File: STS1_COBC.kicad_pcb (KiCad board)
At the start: 4 copper layers, 81 x 85 mm, 207 parts, among them J1 UHF, J16 SWD, Q1 SQ2318, Q2 BSS123, Q3 SQ2318, Q4 SQ2318, U1 W25Q01JVZEIQ, U10 TQP3M9036, U11 NL17SV04XV5T2G, U12 FPF2701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

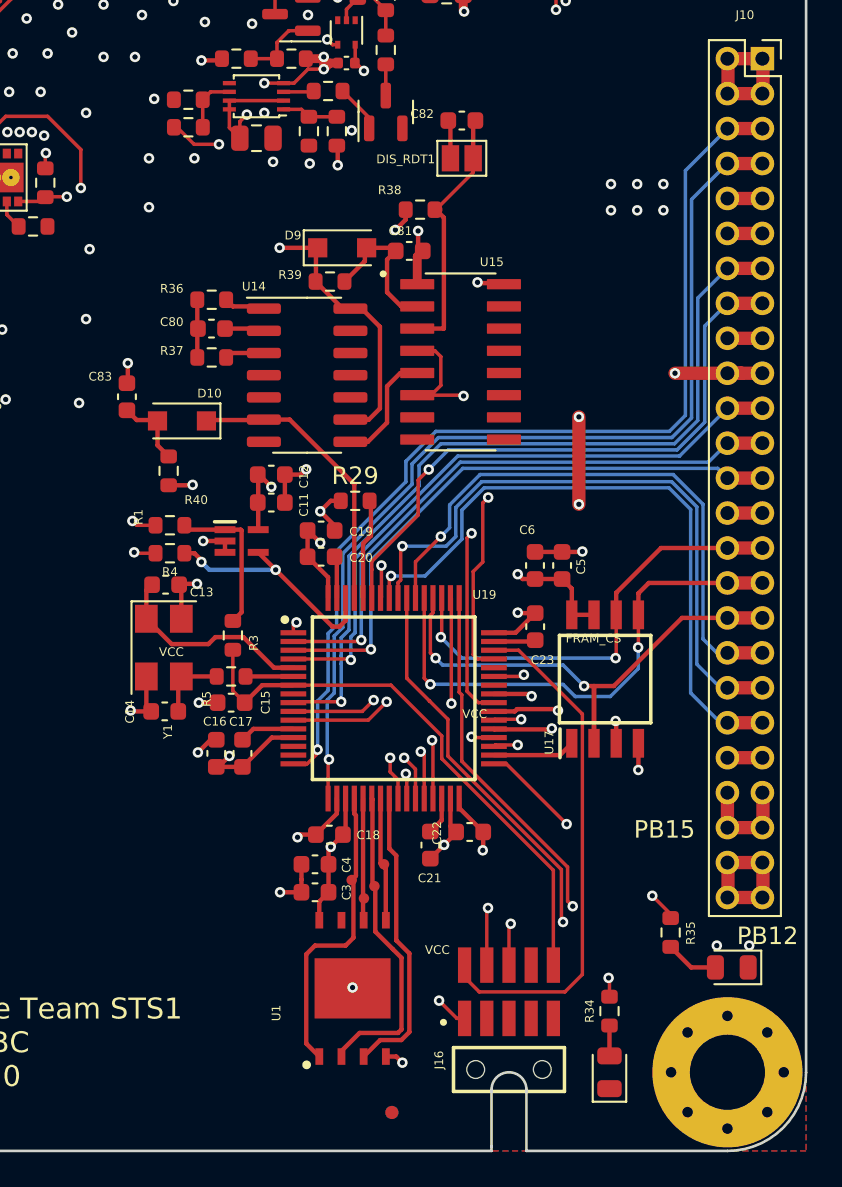
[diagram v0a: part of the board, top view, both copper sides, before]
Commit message: Reorganize silkscreen labels
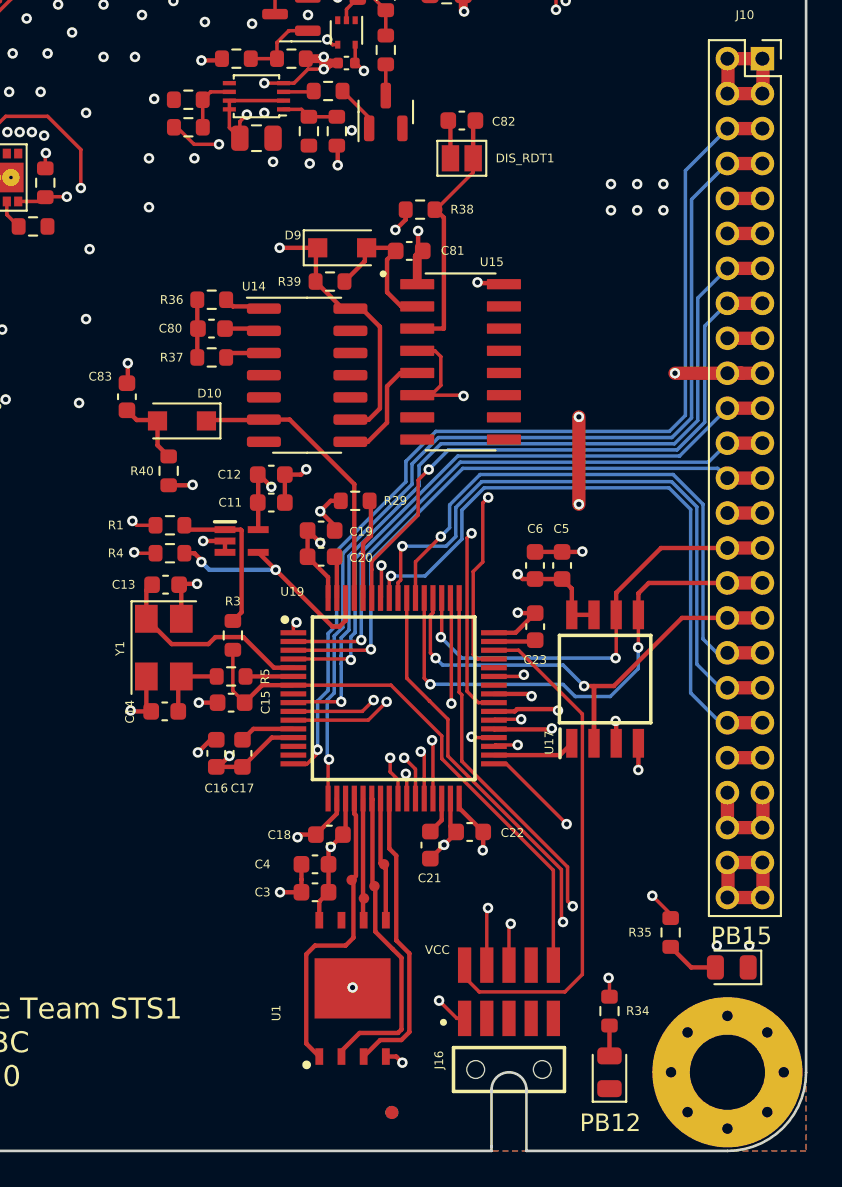
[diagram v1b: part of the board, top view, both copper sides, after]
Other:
- board text removed: "FRAM_CS"
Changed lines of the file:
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@@
     (property "Sheetname" "COBC STM")
     (attr smd)
-    (fp_text reference "Y1" (at 4.81094 -0.2344 90) (layer "F.SilkS")
+    (fp_text reference "Y1" (at 0.05 2.5 90) (layer "F.SilkS")
       (effects (font (size 0.5 0.5) (thickness 0.1)))
     )
@@
     (property "Sheetname" "COBC STM")
     (attr smd)
-    (fp_text reference "R1" (at 1.7985 0.47046 90) (layer "F.SilkS")
+    (fp_text reference "R1" (at 3.1 0 180) (layer "F.SilkS")
       (effects (font (size 0.5 0.5) (thickness 0.1)))
     )
@@
     (property "Sheetname" "COBC STM")
     (attr smd)
-    (fp_text reference "R3" (at 0.43246 -1.1965 90) (layer "F.SilkS")
+    (fp_text reference "R3" (at -1.95 0 180) (layer "F.SilkS")
       (effects (font (size 0.5 0.5) (thickness 0.1)))
     )
@@
     (property "Sheetname" "COBC STM")
     (attr smd)
-    (fp_text reference "C22" (at 1.8655 -0.05746 90) (layer "F.SilkS")
+    (fp_text reference "C22" (at -2.45 -0.05 180) (layer "F.SilkS")
       (effects (font (size 0.5 0.5) (thickness 0.1)))
     )
@@
     (property "Sheetname" "Resetdog")
     (attr smd)
-    (fp_text reference "R37" (at 2.286 0.381) (layer "F.SilkS")
+    (fp_text reference "R37" (at 2.29 -0.0035) (layer "F.SilkS")
       (effects (font (size 0.5 0.5) (thickness 0.1)))
     )
@@
     (property "Sheetname" "Resetdog")
     (attr smd)
-    (fp_text reference "C81" (at -0.508 -1.143) (layer "F.SilkS")
+    (fp_text reference "C81" (at 2.487 -0.0105) (layer "F.SilkS")
       (effects (font (size 0.5 0.5) (thickness 0.1)))
     )
@@
     (property "Sheetname" "COBC STM")
     (attr smd)
-    (fp_text reference "C15" (at 1.9735 -0.01346 90) (layer "F.SilkS")
+    (fp_text reference "C15" (at 1.9735 -0.01346 270) (layer "F.SilkS")
       (effects (font (size 0.5 0.5) (thickness 0.1)))
     )
@@
     (property "Sheetname" "Resetdog")
     (attr smd)
-    (fp_text reference "C82" (at 2.273 0.381) (layer "F.SilkS")
+    (fp_text reference "C82" (at -2.398 -0.059) (layer "F.SilkS")
       (effects (font (size 0.5 0.5) (thickness 0.1)))
     )
@@
     (property "Sheetname" "Resetdog")
     (attr smd)
-    (fp_text reference "C80" (at -2.273 -0.381) (layer "F.SilkS")
+    (fp_text reference "C80" (at -2.347 -0.0055) (layer "F.SilkS")
       (effects (font (size 0.5 0.5) (thickness 0.1)))
     )
@@
     (property "Sheetname" "COBC STM")
     (attr smd)
-    (fp_text reference "C12" (at 1.8635 0.11446 90) (layer "F.SilkS")
+    (fp_text reference "C12" (at -2.4 0 180) (layer "F.SilkS")
       (effects (font (size 0.5 0.5) (thickness 0.1)))
     )
@@
     (property "Sheetname" "COBC Memories")
     (attr smd)
-    (fp_text reference "C5" (at 0.061 -1.0805 90) (layer "F.SilkS")
+    (fp_text reference "C5" (at -2.1 0.04 180) (layer "F.SilkS")
       (effects (font (size 0.5 0.5) (thickness 0.1)))
     )
@@
     (property "Sheetname" "COBC STM")
     (attr smd)
-    (fp_text reference "R34" (at 0 1.1355 90) (layer "F.SilkS")
+    (fp_text reference "R34" (at -0.01 -1.62 180) (layer "F.SilkS")
       (effects (font (size 0.5 0.5) (thickness 0.1)))
     )
@@
     (property "Sheetname" "Resetdog")
     (attr smd)
-    (fp_text reference "R38" (at -1.7394 -1.1176) (layer "F.SilkS")
+    (fp_text reference "R38" (at 2.4052 -0.0083) (layer "F.SilkS")
       (effects (font (size 0.5 0.5) (thickness 0.1)))
     )
@@
     (property "Sheetname" "COBC STM")
     (attr smd)
-    (fp_text reference "C11" (at 1.8635 0.13246 90) (layer "F.SilkS")
+    (fp_text reference "C11" (at -2.35 0 180) (layer "F.SilkS")
       (effects (font (size 0.5 0.5) (thickness 0.1)))
     )
@@
     (property "Sheetname" "Resetdog")
     (attr smd)
-    (fp_text reference "R40" (at 1.6642 -1.5748 180) (layer "F.SilkS")
+    (fp_text reference "R40" (at 0.0143 1.5262 180) (layer "F.SilkS")
       (effects (font (size 0.5 0.5) (thickness 0.1)))
     )
@@
     (property "Sheetname" "COBC Memories")
     (attr smd)
-    (fp_text reference "C3" (at 1.8065 -0.00054 90) (layer "F.SilkS")
+    (fp_text reference "C3" (at -3 0 180) (layer "F.SilkS")
       (effects (font (size 0.5 0.5) (thickness 0.1)))
     )
@@
     (property "exclude_from_bom" "")
     (attr exclude_from_pos_files exclude_from_bom)
-    (fp_text reference "DIS_RDT1" (at -3.2108 0.0529) (layer "F.SilkS")
+    (fp_text reference "DIS_RDT1" (at 3.62 0) (layer "F.SilkS")
       (effects (font (size 0.5 0.5) (thickness 0.1)))
     )
@@
     (property "Sheetname" "COBC STM")
     (attr smd)
-    (fp_text reference "R29" (at 0 -1.43) (layer "F.SilkS")
-      (effects (font (size 1 1) (thickness 0.15)))
+    (fp_text reference "R29" (at 2.3 0) (layer "F.SilkS")
+      (effects (font (size 0.5 0.5) (thickness 0.1)))
     )
     (fp_text value "10K" (at 0 1.43) (layer "F.Fab")
@@
     (property "Sheetname" "COBC STM")
     (attr smd)
-    (fp_text reference "U19" (at 5.19246 -5.925) (layer "F.SilkS")
+    (fp_text reference "U19" (at -5.8 -6.1) (layer "F.SilkS")
       (effects (font (size 0.5 0.5) (thickness 0.1)))
     )
@@
     (property "Sheetname" "COBC STM")
     (attr smd)
-    (fp_text reference "R5" (at 1.3965 -1.28754 90) (layer "F.SilkS")
+    (fp_text reference "R5" (at -1.95 0 270) (layer "F.SilkS")
       (effects (font (size 0.5 0.5) (thickness 0.1)))
     )
@@
     (property "Sheetname" "COBC STM")
     (attr smd)
-    (fp_text reference "C18" (at 2.22446 0.0295) (layer "F.SilkS")
+    (fp_text reference "C18" (at -2.865 0.02) (layer "F.SilkS")
       (effects (font (size 0.5 0.5) (thickness 0.1)))
     )
@@
     (property "Sheetname" "COBC STM")
     (attr smd)
-    (fp_text reference "R4" (at 0 -1.0685) (layer "F.SilkS")
+    (fp_text reference "R4" (at 3.1 0) (layer "F.SilkS")
       (effects (font (size 0.5 0.5) (thickness 0.1)))
     )
@@
     (property "Sheetname" "COBC STM")
     (attr smd)
-    (fp_text reference "C23" (at 1.9099 -0.41846) (layer "F.SilkS")
+    (fp_text reference "C23" (at 1.9 0) (layer "F.SilkS")
       (effects (font (size 0.5 0.5) (thickness 0.1)))
     )
@@
     (property "Sheetname" "COBC Memories")
     (attr smd)
-    (fp_text reference "C4" (at 1.8065 0.03046 90) (layer "F.SilkS")
+    (fp_text reference "C4" (at -3 0 180) (layer "F.SilkS")
       (effects (font (size 0.5 0.5) (thickness 0.1)))
     )
@@
     (property "Sheetname" "Resetdog")
     (attr smd)
-    (fp_text reference "R36" (at 2.286 0.635) (layer "F.SilkS")
+    (fp_text reference "R36" (at 2.29 -0.0055) (layer "F.SilkS")
       (effects (font (size 0.5 0.5) (thickness 0.1)))
     )
@@
     (property "Sheetname" "COBC STM")
     (attr smd)
-    (fp_text reference "C13" (at -2.06446 -0.4295 180) (layer "F.SilkS")
+    (fp_text reference "C13" (at 2.4 0 180) (layer "F.SilkS")
       (effects (font (size 0.5 0.5) (thickness 0.1)))
     )
@@
     (property "Sheetname" "Resetdog")
     (attr smd)
-    (fp_text reference "R39" (at -2.286 -0.381) (layer "F.SilkS")
+    (fp_text reference "R39" (at -2.3196 0.0069) (layer "F.SilkS")
       (effects (font (size 0.5 0.5) (thickness 0.1)))
     )
@@
     (property "Sheetname" "COBC STM")
     (attr smd)
-    (fp_text reference "R35" (at 0.035 -1.1505 90) (layer "F.SilkS")
+    (fp_text reference "R35" (at 0 1.75 180) (layer "F.SilkS")
       (effects (font (size 0.5 0.5) (thickness 0.1)))
     )
@@
     (property "Sheetname" "COBC STM")
     (attr smd)
-    (fp_text reference "C16" (at 1.8205 -0.07954 180) (layer "F.SilkS")
+    (fp_text reference "C16" (at -2 0 180) (layer "F.SilkS")
       (effects (font (size 0.5 0.5) (thickness 0.1)))
     )
@@
     (property "Sheetname" "COBC Memories")
     (attr smd)
-    (fp_text reference "C6" (at -2.032 0.4455) (layer "F.SilkS")
+    (fp_text reference "C6" (at -2.1 -0.01) (layer "F.SilkS")
       (effects (font (size 0.5 0.5) (thickness 0.1)))
     )
@@
     (property "Sheetname" "COBC STM")
     (attr smd)
-    (fp_text reference "C17" (at -1.8105 0.08754) (layer "F.SilkS")
+    (fp_text reference "C17" (at 2 0) (layer "F.SilkS")
       (effects (font (size 0.5 0.5) (thickness 0.1)))
     )
@@
     (effects (font (size 1.2 1.2) (thickness 0.2)))
   )
-  (gr_text "PB15" (at 187.898 108.6104) (layer "F.SilkS")
+  (gr_text "PB15" (at 192.3 114.7) (layer "F.SilkS")
     (effects (font (size 1 1) (thickness 0.15)))
   )
-  (gr_text "VCC" (at 177.03254 102) (layer "F.SilkS")
-    (effects (font (size 0.5 0.5) (thickness 0.1)))
-  )
-  (gr_text "FRAM_CS" (at 183.837 97.6755) (layer "F.SilkS")
-    (effects (font (size 0.5 0.5) (thickness 0.1)))
-  )
   (gr_text "3V3" (at 138.368 91.276) (layer "F.SilkS")
     (effects (font (size 1 1) (thickness 0.15)))
   )
-  (gr_text "PB12" (at 193.8 114.7) (layer "F.SilkS")
+  (gr_text "PB12" (at 184.8 125.4) (layer "F.SilkS")
     (effects (font (size 1 1) (thickness 0.15)))
   )
@@
     (effects (font (size 1 1) (thickness 0.15)))
   )
-  (gr_text "VCC" (at 159.68254 98.45) (layer "F.SilkS")
-    (effects (font (size 0.5 0.5) (thickness 0.1)))
-  )
   (gr_text "VCC" (at 174.9 115.5) (layer "F.SilkS")
     (effects (font (size 0.5 0.5) (thickness 0.1)))
@@
   (segment (start 117.4 92.5) (end 119.4 92.5) (width 0.762) (layer "F.Cu") (net 157))
   (segment (start 191.53254 74.5) (end 193.53254 74.5) (width 0.762) (layer "F.Cu") (net 158))
-  (segment (start 174.6 103.5) (end 174.6 103.6) (width 0.2) (layer "F.Cu") (net 163))
   (segment (start 174.65 103.55) (end 174.65 106.838) (width 0.2) (layer "F.Cu") (net 163))
   (segment (start 117.4 88.5) (end 119.4 88.5) (width 0.762) (layer "F.Cu") (net 163))
-  (segment (start 174.6 103.6) (end 174.5524 103.6476) (width 0.2) (layer "F.Cu") (net 163))
   (via (at 174.6 103.5) (size 0.6) (drill 0.3) (layers "F.Cu" "B.Cu") (net 163))
   (segment (start 174.6 103.5) (end 174.5 103.6) (width 0.2) (layer "In2.Cu") (net 163))
